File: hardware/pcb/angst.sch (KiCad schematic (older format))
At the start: 86 parts, among them J1 USB_B_Micro, J2 Conn_02x05_Odd_Even, J3 BATT, J4 Conn_01x03, J5 Conn_01x03, J6 Conn_01x03, Q1 IRLML6401TRPBF, SW1 SW_Push, U1 STM32F303RETx, U2 M24C02-RDW, U3 STSPIN233, U4 STSPIN233, U5 TLV1117-50, U6 STSPIN233, U7 TLV1117-33, Y1 Crystal_GND24

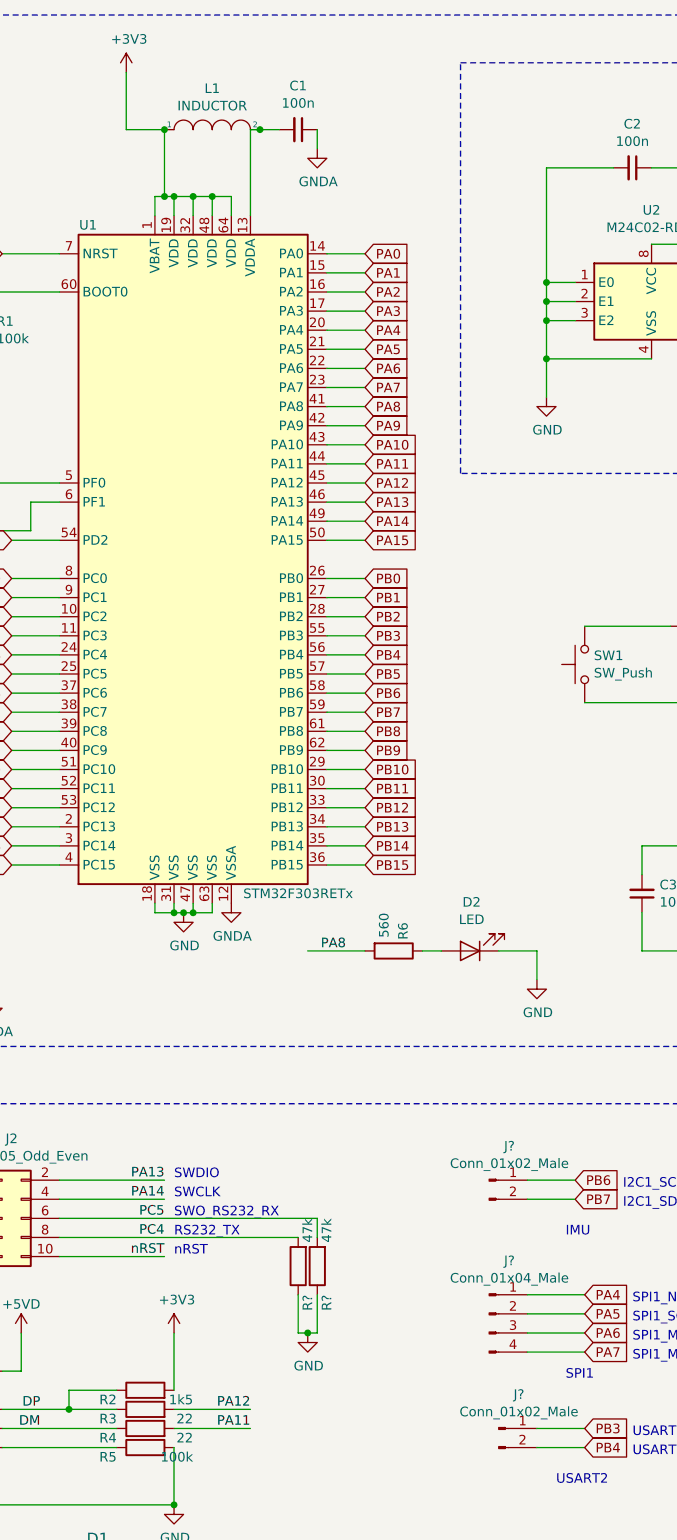
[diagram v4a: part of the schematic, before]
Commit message: Add bead footprint
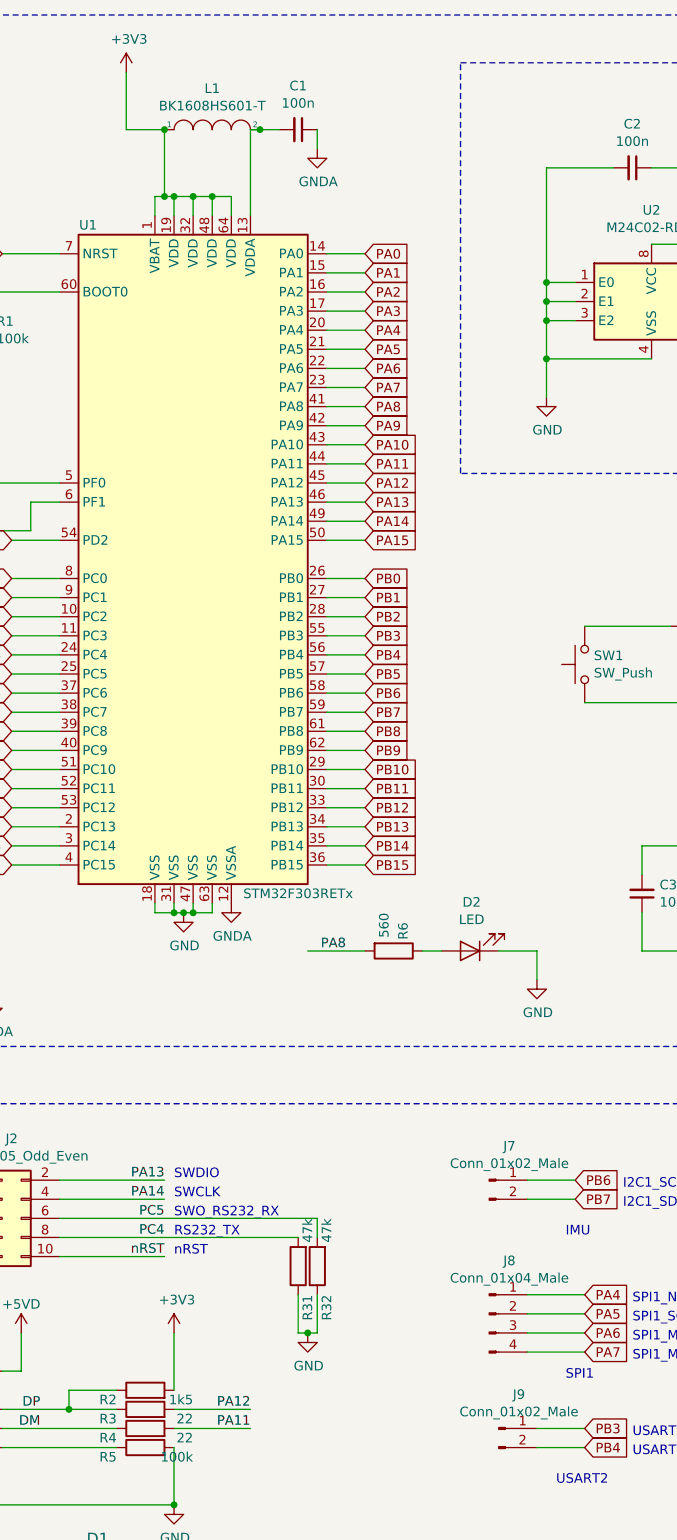
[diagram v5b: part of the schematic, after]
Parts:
- J2: footprint (none) -> Connector_Harwin:Harwin_Gecko-G125-FVX1005L0X_2x05_P1.25mm_Vertical
- J4, J5, J6: footprint (none) -> Connector_JST:JST_EH_B3B-EH-A_1x03_P2.50mm_Vertical
- J7, J9: renamed from J?; footprint (none) -> Connector_JST:JST_EH_B2B-EH-A_1x02_P2.50mm_Vertical
- J8: renamed from J?; footprint (none) -> Connector_JST:JST_EH_B4B-EH-A_1x04_P2.50mm_Vertical
- L1: value INDUCTOR -> BK1608HS601-T; footprint (none) -> Inductor_SMD:L_0603_1608Metric_Pad1.05x0.95mm_HandSolder
- gave numbers to parts that had none: 2
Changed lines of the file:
@@
 P 3100 1450
 F 0 "L1" H 3100 1665 50  0000 C CNN
-F 1 "INDUCTOR" H 3100 1574 50  0000 C CNN
-F 2 "" H 3100 1450 50  0001 C CNN
+F 1 "BK1608HS601-T" H 3100 1574 50  0000 C CNN
+F 2 "Inductor_SMD:L_0603_1608Metric_Pad1.05x0.95mm_HandSolder" H 3100 1450 50  0001 C CNN
 F 3 "~" H 3100 1450 50  0001 C CNN
 	1    3100 1450
@@
 F 0 "J5" H 12730 4442 50  0000 L CNN
 F 1 "Conn_01x03" H 12730 4351 50  0000 L CNN
-F 2 "" H 12650 4400 50  0001 C CNN
+F 2 "Connector_JST:JST_EH_B3B-EH-A_1x03_P2.50mm_Vertical" H 12650 4400 50  0001 C CNN
 F 3 "~" H 12650 4400 50  0001 C CNN
 	1    12650 4400
@@
 F 0 "J4" H 10930 2292 50  0000 L CNN
 F 1 "Conn_01x03" H 10930 2201 50  0000 L CNN
-F 2 "" H 10850 2250 50  0001 C CNN
+F 2 "Connector_JST:JST_EH_B3B-EH-A_1x03_P2.50mm_Vertical" H 10850 2250 50  0001 C CNN
 F 3 "~" H 10850 2250 50  0001 C CNN
 	1    10850 2250
@@
 F 0 "J6" H 14130 2242 50  0000 L CNN
 F 1 "Conn_01x03" H 14130 2151 50  0000 L CNN
-F 2 "" H 14050 2200 50  0001 C CNN
+F 2 "Connector_JST:JST_EH_B3B-EH-A_1x03_P2.50mm_Vertical" H 14050 2200 50  0001 C CNN
 F 3 "~" H 14050 2200 50  0001 C CNN
 	1    14050 2200
@@
 F 0 "J2" H 2050 7567 50  0000 C CNN
 F 1 "Conn_02x05_Odd_Even" H 2050 7476 50  0000 C CNN
-F 2 "" H 2000 7150 50  0001 C CNN
+F 2 "Connector_Harwin:Harwin_Gecko-G125-FVX1005L0X_2x05_P1.25mm_Vertical" H 2000 7150 50  0001 C CNN
 F 3 "~" H 2000 7150 50  0001 C CNN
 	1    2000 7150
@@
 $EndComp
 $Comp
-L Device:R R?
+L Device:R R32
 U 1 1 5CD3D3C1
 P 3650 7400
-F 0 "R?" V 3600 7550 50  0000 L CNN
+F 0 "R32" V 3600 7550 50  0000 L CNN
 F 1 "47k" V 3600 7150 50  0000 L CNN
 F 2 "Resistor_SMD:R_0603_1608Metric_Pad1.05x0.95mm_HandSolder" V 3580 7400 50  0001 C CNN
@@
 $EndComp
 $Comp
-L Device:R R?
+L Device:R R31
 U 1 1 5CD7F8BD
 P 3550 7400
-F 0 "R?" V 3500 7550 50  0000 L CNN
+F 0 "R31" V 3500 7550 50  0000 L CNN
 F 1 "47k" V 3500 7150 50  0000 L CNN
 F 2 "Resistor_SMD:R_0603_1608Metric_Pad1.05x0.95mm_HandSolder" V 3480 7400 50  0001 C CNN
@@
 	3600 7750 3650 7750
 $Comp
-L Connector:Conn_01x02_Male J?
+L Connector:Conn_01x02_Male J7
 U 1 1 5CDE63FD
 P 4550 6950
-F 0 "J?" H 4656 7128 50  0000 C CNN
+F 0 "J7" H 4656 7128 50  0000 C CNN
 F 1 "Conn_01x02_Male" H 4656 7037 50  0000 C CNN
-F 2 "" H 4550 6950 50  0001 C CNN
+F 2 "Connector_JST:JST_EH_B2B-EH-A_1x02_P2.50mm_Vertical" H 4550 6950 50  0001 C CNN
 F 3 "~" H 4550 6950 50  0001 C CNN
 	1    4550 6950
@@
 	6950 6550 1100 6550
 $Comp
-L Connector:Conn_01x04_Male J?
+L Connector:Conn_01x04_Male J8
 U 1 1 5CE79D49
 P 4550 7650
-F 0 "J?" H 4656 7928 50  0000 C CNN
+F 0 "J8" H 4656 7928 50  0000 C CNN
 F 1 "Conn_01x04_Male" H 4656 7837 50  0000 C CNN
-F 2 "" H 4550 7650 50  0001 C CNN
+F 2 "Connector_JST:JST_EH_B4B-EH-A_1x04_P2.50mm_Vertical" H 4550 7650 50  0001 C CNN
 F 3 "~" H 4550 7650 50  0001 C CNN
 	1    4550 7650
@@
 SPI1_MOSI
 $Comp
-L Connector:Conn_01x02_Male J?
+L Connector:Conn_01x02_Male J9
 U 1 1 5CF0A01D
 P 4600 8250
-F 0 "J?" H 4706 8428 50  0000 C CNN
+F 0 "J9" H 4706 8428 50  0000 C CNN
 F 1 "Conn_01x02_Male" H 4706 8337 50  0000 C CNN
-F 2 "" H 4600 8250 50  0001 C CNN
+F 2 "Connector_JST:JST_EH_B2B-EH-A_1x02_P2.50mm_Vertical" H 4600 8250 50  0001 C CNN
 F 3 "~" H 4600 8250 50  0001 C CNN
 	1    4600 8250
@@
 SPI1
 $Comp
-L power:GND #PWR?
+L power:GND #PWR053
 U 1 1 5CF30178
 P 1750 6000
-F 0 "#PWR?" H 1750 5750 50  0001 C CNN
+F 0 "#PWR053" H 1750 5750 50  0001 C CNN
 F 1 "GND" H 1755 5827 50  0000 C CNN
 F 2 "" H 1750 6000 50  0001 C CNN
@@
 $EndComp
 $Comp
-L power:GNDA #PWR?
+L power:GNDA #PWR054
 U 1 1 5CF3022F
 P 1950 6000
-F 0 "#PWR?" H 1950 5750 50  0001 C CNN
+F 0 "#PWR054" H 1950 5750 50  0001 C CNN
 F 1 "GNDA" H 1955 5827 50  0000 C CNN
 F 2 "" H 1950 6000 50  0001 C CNN

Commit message: Start work on PCB layout
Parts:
- removed J3: BATT, symbol Connector_Generic:Conn_02x01_Row_Letter_Last
- added J3: Conn_01x02_Male, Connector_JST:JST_EH_B2B-EH-A_1x02_P2.50mm_Vertical, symbol Connector:Conn_01x02_Male
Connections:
- net GND: now also J3.2 (Pin_2)
- net OUTW_1: now reaches J4.3 (Pin_3), U3.10 (OUTW)
- net OUTU_1: now reaches J4.1 (Pin_1), U3.3 (OUTU)
- net OUTV_1: now reaches J4.2 (Pin_2), U3.7 (OUTV)
- net at Q1.3 (D): now also J3.1 (Pin_1)
- net OUTW_2: now reaches J5.3 (Pin_3), U4.10 (OUTW)
- net OUTU_2: now reaches J5.1 (Pin_1), U4.3 (OUTU)
- net OUTV_2: now reaches J5.2 (Pin_2), U4.7 (OUTV)
- net OUTW_3: now reaches J6.3 (Pin_3), U6.10 (OUTW)
- net OUTU_3: now reaches J6.1 (Pin_1), U6.3 (OUTU)
- net OUTV_3: now reaches J6.2 (Pin_2), U6.7 (OUTV)
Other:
- moved on the sheet: J4, J5, J6
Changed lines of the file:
@@
 L Connector_Generic:Conn_01x03 J5
 U 1 1 5CC92982
-P 12650 4400
-F 0 "J5" H 12730 4442 50  0000 L CNN
-F 1 "Conn_01x03" H 12730 4351 50  0000 L CNN
-F 2 "Connector_JST:JST_EH_B3B-EH-A_1x03_P2.50mm_Vertical" H 12650 4400 50  0001 C CNN
-F 3 "~" H 12650 4400 50  0001 C CNN
-	1    12650 4400
+P 12800 4400
+F 0 "J5" H 12880 4442 50  0000 L CNN
+F 1 "Conn_01x03" H 12880 4351 50  0000 L CNN
+F 2 "Connector_JST:JST_EH_B3B-EH-A_1x03_P2.50mm_Vertical" H 12800 4400 50  0001 C CNN
+F 3 "~" H 12800 4400 50  0001 C CNN
+	1    12800 4400
 	1    0    0    -1
 $EndComp
@@
 L Connector_Generic:Conn_01x03 J4
 U 1 1 5CC93F81
-P 10850 2250
-F 0 "J4" H 10930 2292 50  0000 L CNN
-F 1 "Conn_01x03" H 10930 2201 50  0000 L CNN
-F 2 "Connector_JST:JST_EH_B3B-EH-A_1x03_P2.50mm_Vertical" H 10850 2250 50  0001 C CNN
-F 3 "~" H 10850 2250 50  0001 C CNN
-	1    10850 2250
+P 11000 2250
+F 0 "J4" H 11080 2292 50  0000 L CNN
+F 1 "Conn_01x03" H 11080 2201 50  0000 L CNN
+F 2 "Connector_JST:JST_EH_B3B-EH-A_1x03_P2.50mm_Vertical" H 11000 2250 50  0001 C CNN
+F 3 "~" H 11000 2250 50  0001 C CNN
+	1    11000 2250
 	1    0    0    -1
 $EndComp
@@
 L Connector_Generic:Conn_01x03 J6
 U 1 1 5CC94D02
-P 14050 2200
-F 0 "J6" H 14130 2242 50  0000 L CNN
-F 1 "Conn_01x03" H 14130 2151 50  0000 L CNN
-F 2 "Connector_JST:JST_EH_B3B-EH-A_1x03_P2.50mm_Vertical" H 14050 2200 50  0001 C CNN
-F 3 "~" H 14050 2200 50  0001 C CNN
-	1    14050 2200
-	1    0    0    -1
-$EndComp
-Wire Wire Line
-	10650 2150 10550 2150
-Wire Wire Line
-	10650 2250 10550 2250
-Wire Wire Line
-	10650 2350 10550 2350
-Wire Wire Line
-	13850 2300 13750 2300
-Wire Wire Line
-	13850 2200 13750 2200
-Wire Wire Line
-	13850 2100 13750 2100
-Wire Wire Line
-	12450 4500 12300 4500
-Wire Wire Line
-	12450 4400 12300 4400
-Wire Wire Line
-	12450 4300 12300 4300
+P 14250 2200
+F 0 "J6" H 14330 2242 50  0000 L CNN
+F 1 "Conn_01x03" H 14330 2151 50  0000 L CNN
+F 2 "Connector_JST:JST_EH_B3B-EH-A_1x03_P2.50mm_Vertical" H 14250 2200 50  0001 C CNN
+F 3 "~" H 14250 2200 50  0001 C CNN
+	1    14250 2200
+	1    0    0    -1
+$EndComp
+Wire Wire Line
+	10800 2150 10550 2150
+Wire Wire Line
+	10800 2250 10550 2250
+Wire Wire Line
+	10800 2350 10550 2350
+Wire Wire Line
+	12600 4500 12300 4500
+Wire Wire Line
+	12600 4400 12300 4400
+Wire Wire Line
+	12600 4300 12300 4300
 Wire Notes Line
 	8000 850  14750 850
@@
 Text Label 2850 7350 2    50   ~ 0
 nRST
-$Comp
-L Connector_Generic:Conn_02x01_Row_Letter_Last J3
-U 1 1 5CF59E6C
-P 8700 8050
-F 0 "J3" V 8704 8130 50  0000 L CNN
-F 1 "BATT" H 8650 7950 50  0000 L CNN
-F 2 "" H 8700 8050 50  0001 C CNN
-F 3 "~" H 8700 8050 50  0001 C CNN
-	1    8700 8050
-	0    1    1    0
-$EndComp
 Wire Wire Line
 	8700 8350 8950 8350
@@
 Text Notes 6500 10450 0    50   ~ 0
 Connector
+$Comp
+L Connector:Conn_01x02_Male J3
+U 1 1 5CBBF2C8
+P 8500 8050
+F 0 "J3" H 8550 8250 50  0000 C CNN
+F 1 "Conn_01x02_Male" H 8350 8150 50  0000 C CNN
+F 2 "Connector_JST:JST_EH_B2B-EH-A_1x02_P2.50mm_Vertical" H 8500 8050 50  0001 C CNN
+F 3 "~" H 8500 8050 50  0001 C CNN
+	1    8500 8050
+	1    0    0    -1
+$EndComp
+Wire Wire Line
+	8700 7850 8700 8050
+Wire Wire Line
+	8700 8150 8700 8350
+Wire Wire Line
+	13750 2100 14050 2100
+Wire Wire Line
+	13750 2200 14050 2200
+Wire Wire Line
+	13750 2300 14050 2300
+Text Label 12350 4300 0    50   ~ 0
+OUTU_2
+Text Label 12350 4400 0    50   ~ 0
+OUTV_2
+Text Label 12350 4500 0    50   ~ 0
+OUTW_2
+Text Label 13800 2100 0    50   ~ 0
+OUTU_3
+Text Label 13800 2200 0    50   ~ 0
+OUTV_3
+Text Label 13800 2300 0    50   ~ 0
+OUTW_3
+Text Label 10550 2150 0    50   ~ 0
+OUTU_1
+Text Label 10550 2250 0    50   ~ 0
+OUTV_1
+Text Label 10550 2350 0    50   ~ 0
+OUTW_1
 $EndSCHEMATC
